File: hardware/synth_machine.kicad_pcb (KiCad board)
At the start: 2 copper layers, 234.9 x 161.9 mm, 90 parts, among them J1 USB-C (MIDI + 5V power), J10 Pot Wave (10k lin, panel moun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, J11 Pot Attack (10k lin, panel mo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, J12 Pot Decay (10k lin, panel mou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, J13 Pot Sustain (10k lin, panel m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, J14 Pot Release (10k lin, panel m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, J3 Panel power switch, J4 From amp screw terminals (L+ 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, J5 Speaker L (JST-PH), J6 Speaker R (JST-PH), J7 Headphones 3.5mm (CUI SJ1-351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, J8 Expansion, J9 Panel LED (anode, cathode), Q1 2N3904, SW1 KEY C4 (direct D10) - 2x Keys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, SW10 D#4 [c4 r1] - 2x Keystone 3534, SW11 F#4 [c3 r1] - 2x Keystone 3534, SW12 G#4 [c2 r1] - 2x Keystone 3534, SW13 A#4 [c1 r1] - 2x Keystone 3534, SW14 BTN1 [c0 r0] - 2x Keystone 35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, SW15 BTN2 [c0 r1] - 2x Keystone 35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, SW16 BTN3 [c1 r0] - 2x Keystone 35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, SW17 BTN4 [c2 r0] - 2x Keystone 35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, SW18 BTN5 [c3 r0] - 2x Keystone 35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, SW19 BTN6 [c4 r0] - 2x Keystone 35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, SW2 D4 [c5 r1] - 2x Keystone 3534, SW3 E4 [c5 r2] - 2x Keystone 3534, SW4 F4 [c4 r2] - 2x Keystone 3534, SW5 G4 [c3 r2] - 2x Keystone 3534, SW6 A4 [c2 r2] - 2x Keystone 3534, SW7 B4 [c1 r2] - 2x Keystone 3534, SW8 C5 [c0 r2] - 2x Keystone 3534, SW9 C#4 [c5 r0] - 2x Keystone 3534, U1 Daisy Seed, U2 TPA6138A2PWR

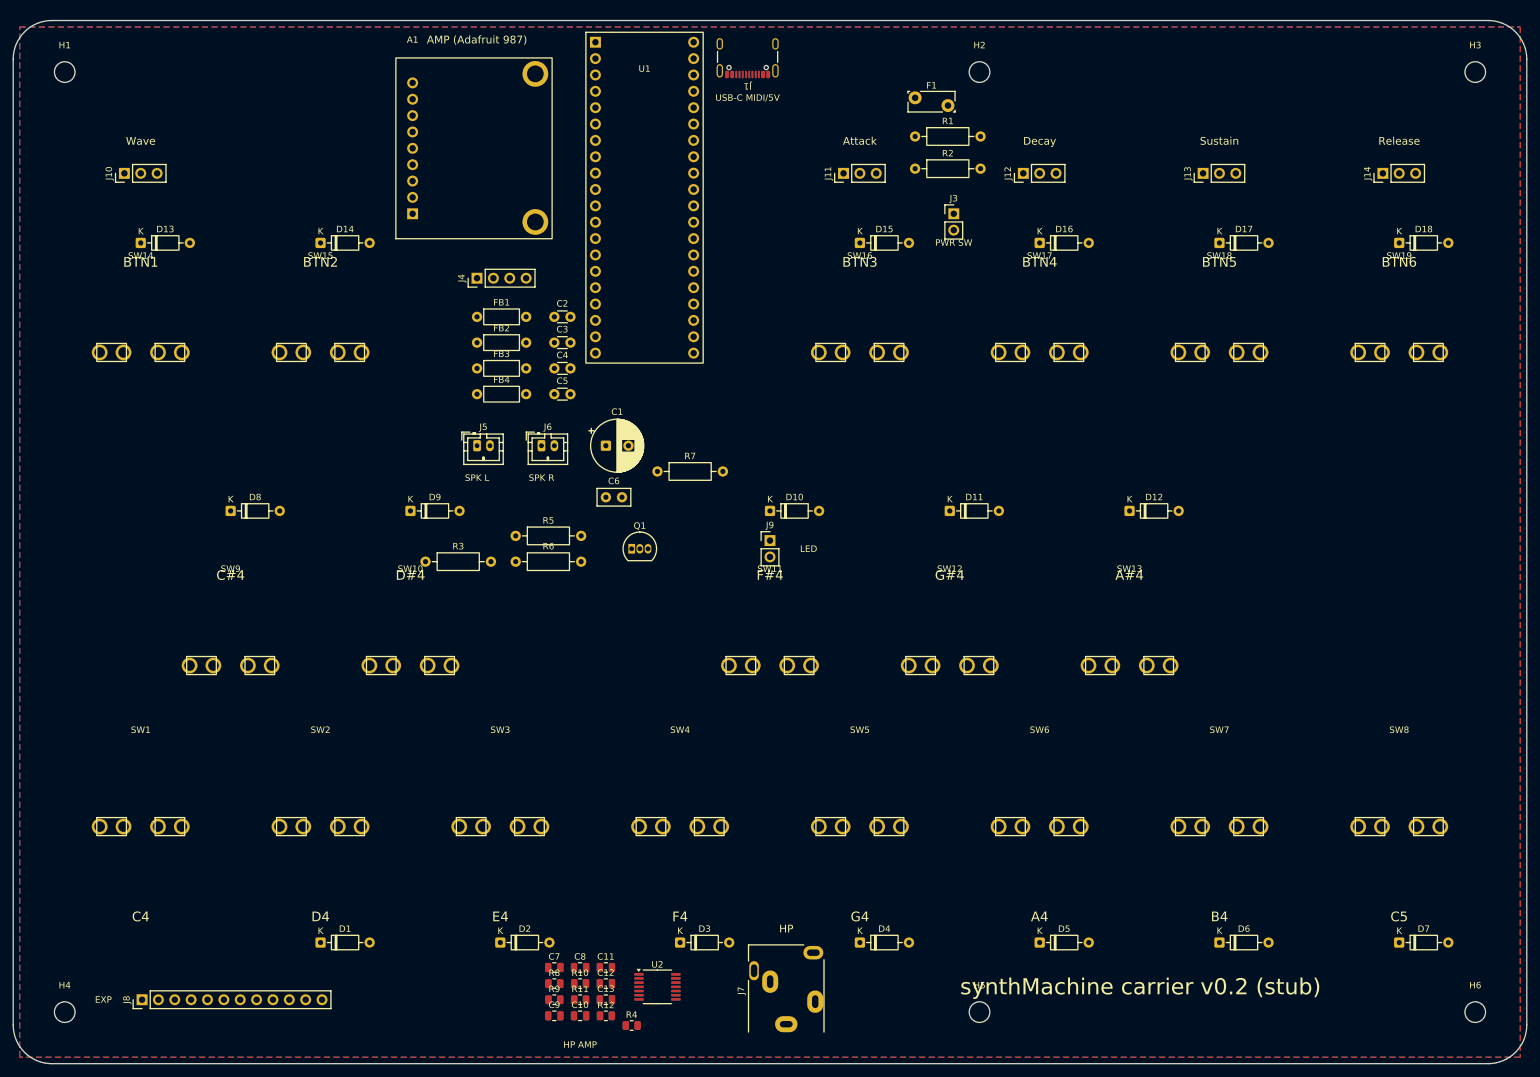
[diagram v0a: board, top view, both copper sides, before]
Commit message: Route the carrier board and fix the button tab pitch
- Button tab pitch measured 9.05 mm outer-to-outer (2.8 mm tabs), so the
  Keystone 3534 receptacle pairs now sit on 6.25 mm centres
- hardware/route.py: Specctra export -> Freerouting (headless, Java 25) ->
  session import -> GND pours on both layers -> fill.  Pours are stripped
  before export so GND is routed with real tracks/vias
- Net classes: 0.25 mm default, 0.6 mm Power (+5V, speaker lines),
  0.4 mm USB_Power for VBUS
- Board is fully routed: 781 segments, 46 vias, 0 unrouted, DRC clean
  apart from USB-C library hole-clearance nits and two thermal-spoke notes

Co-Authored-By: Claude Fable 5.1 <noreply@anthropic.com>
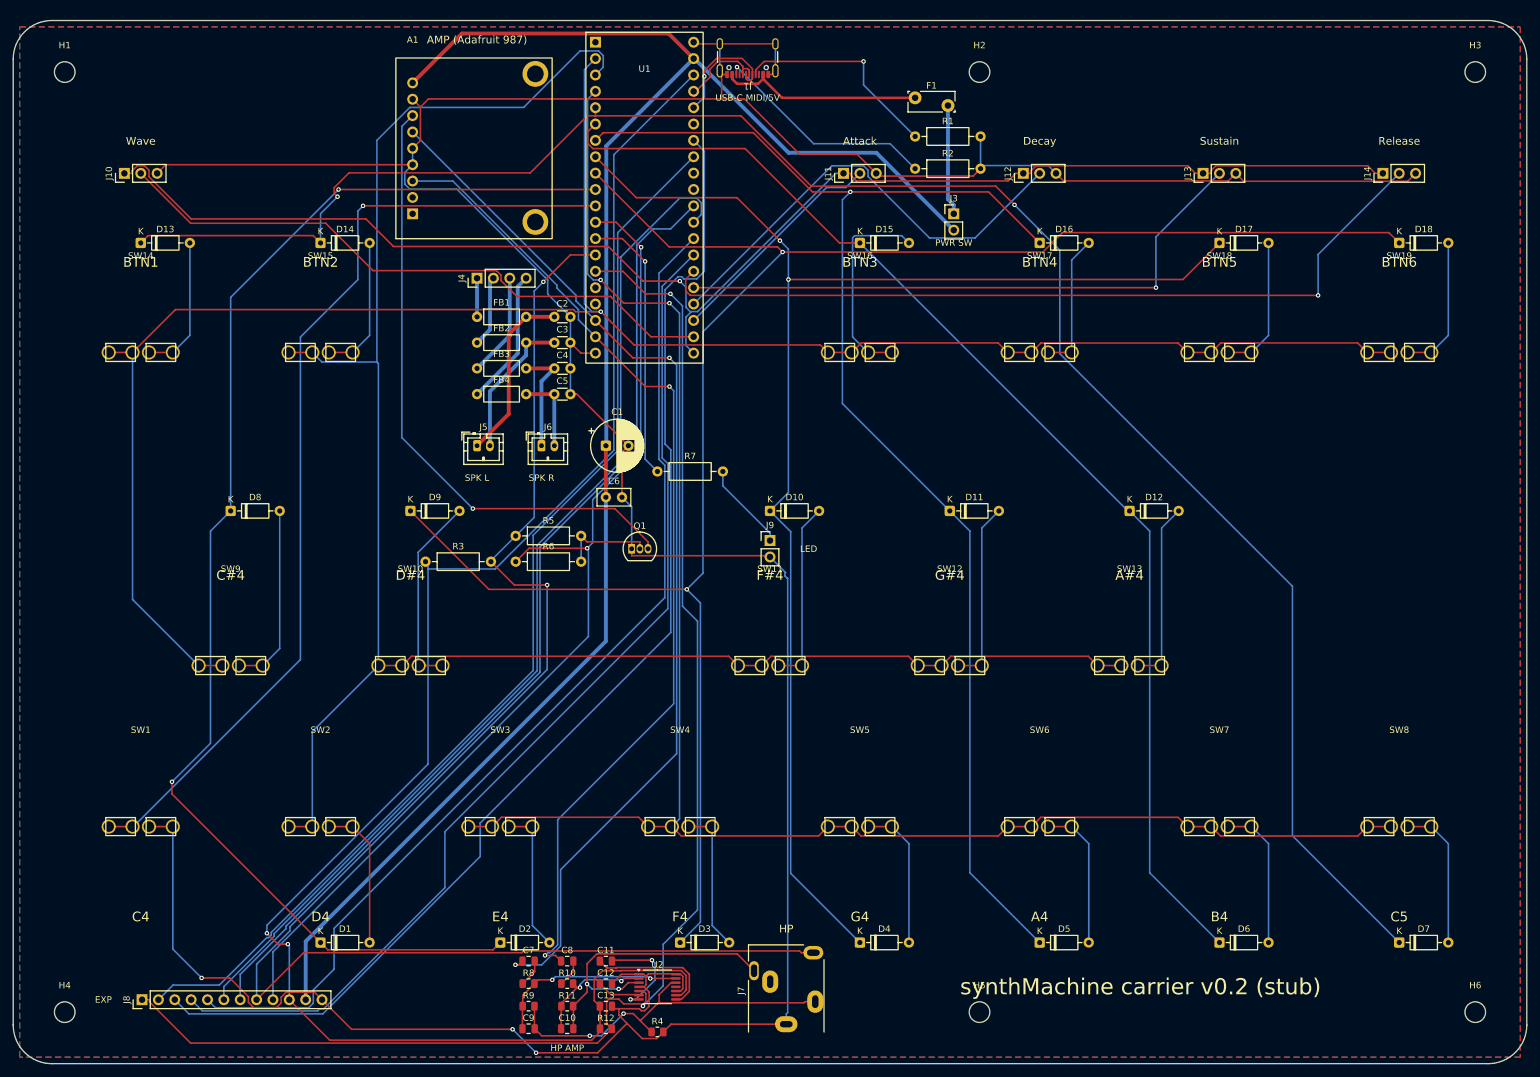
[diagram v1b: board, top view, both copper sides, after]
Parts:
- moved C9 4.47 mm to (80.0, 156.5)
- moved C7 4.12 mm to (80.0, 146.0)
- moved R4 4.12 mm to (100.0, 157.0)
- moved R9 4.12 mm to (80.0, 153.0)
- moved R8 4.00 mm to (80.0, 149.5)
- moved C10 2.83 mm to (86.0, 156.5)
- moved C8 2.24 mm to (86.0, 146.0)
- moved R11 2.24 mm to (86.0, 153.0)
- moved R10 2.00 mm to (86.0, 149.5)
- moved R12 2.00 mm to (92.0, 156.5)
- moved C11 1.00 mm to (92.0, 146.0)
- moved C13 1.00 mm to (92.0, 153.0)
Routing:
- net GND: track 0.00 -> 590.3 mm, vias 0 -> 3
- net ROW0: track 0.00 -> 306.6 mm, vias 0 -> 1
- net COL4: track 0.00 -> 295.2 mm, vias 0 -> 2
- net COL0: track 0.00 -> 295.2 mm, vias 0 -> 2
- net ROW1: track 0.00 -> 292.5 mm
- net ROW2: track 0.00 -> 275.1 mm, vias 0 -> 2
- net +5V: track 0.00 -> 270.9 mm
- net +3V3: track 0.00 -> 260.0 mm, vias 0 -> 2
- net HP_DET: track 0.00 -> 239.6 mm, vias 0 -> 2
- net +3.3VA: track 0.00 -> 227.5 mm, vias 0 -> 1
- net HP_MUTE: track 0.00 -> 219.8 mm, vias 0 -> 2
- net COL3: track 0.00 -> 219.8 mm, vias 0 -> 2
- net COL2: track 0.00 -> 206.3 mm, vias 0 -> 1
- net COL5: track 0.00 -> 205.9 mm, vias 0 -> 2
- net EXP_D27: track 0.00 -> 187.6 mm
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
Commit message: Seat the USB-C receptacle on the board edge, harden route.py
- J1 moved so the footprint's "PCB Edge" guide line sits on the outline
  (shell overhangs ~1 mm as intended); board re-routed, still 0 unrouted
- route.py runs the pour step in a fresh interpreter (SWIG ownership crash
  when reloading the board in the same process)
- README: connector-edge check added to the pre-order list

Co-Authored-By: Claude Fable 5.1 <noreply@anthropic.com>
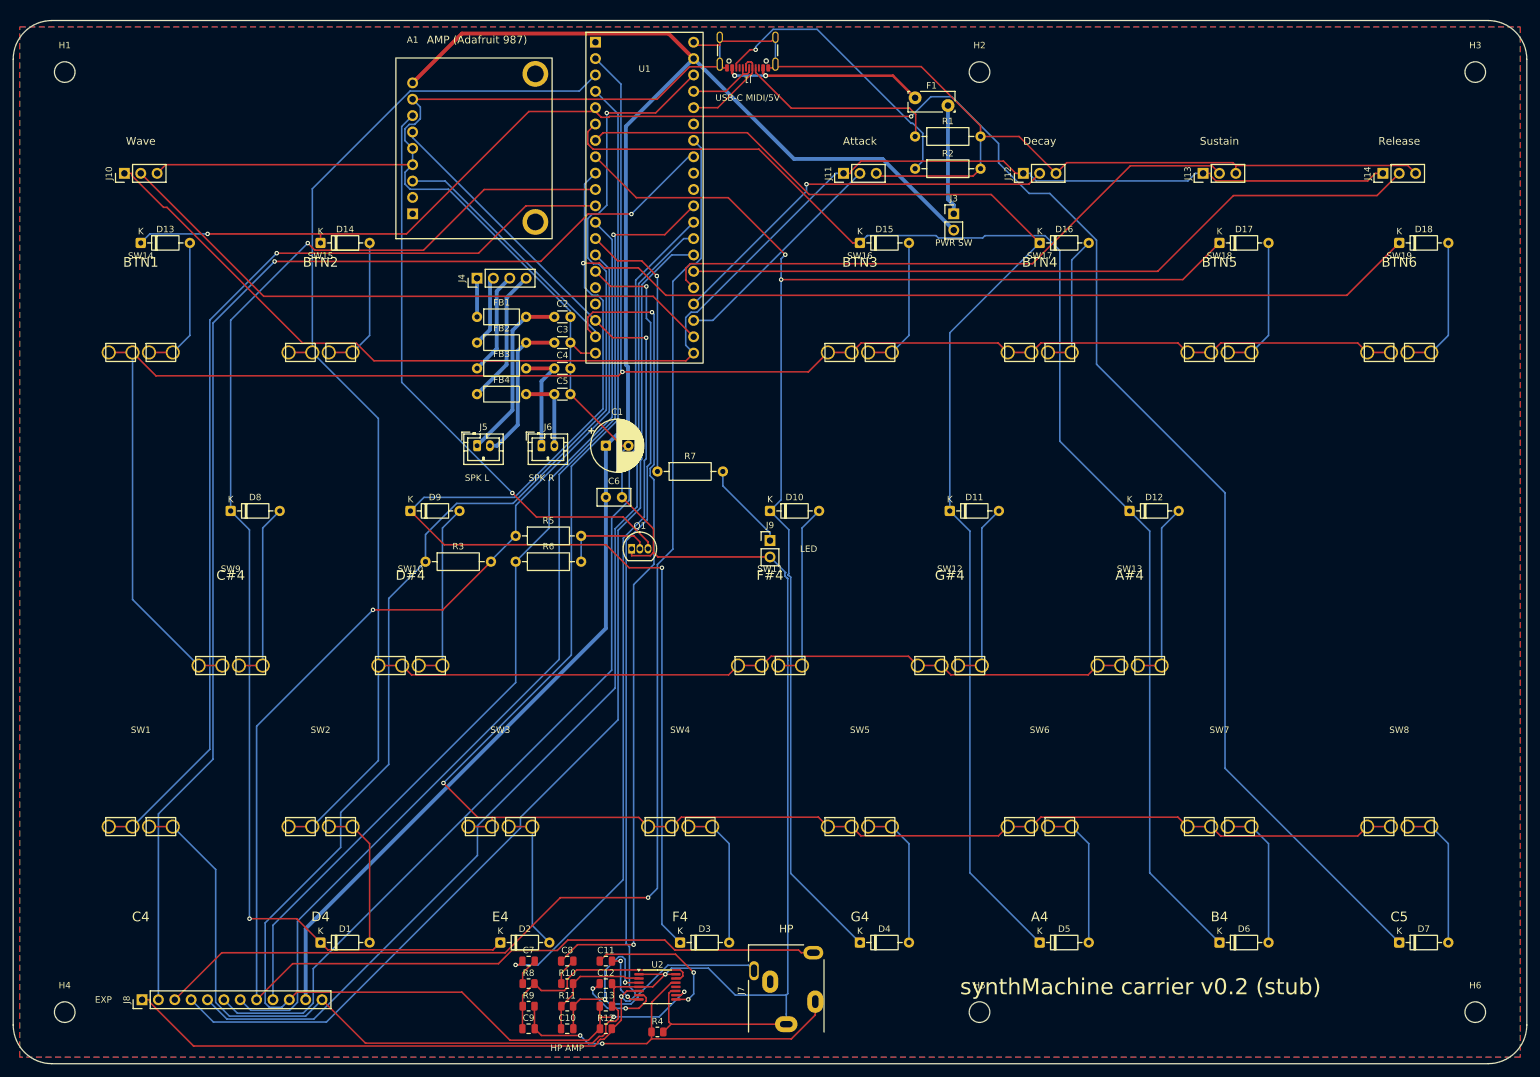
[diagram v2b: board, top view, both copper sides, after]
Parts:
- moved J1 1.03 mm to (114.0, 3.67)
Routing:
- net EXP_D26: track 169.6 -> 193.8 mm, vias 0 -> 2
- net GND: track 590.3 -> 613.7 mm, vias 3 -> 1
- net COL1: track 184.0 -> 202.6 mm
- net MUTE: track 161.3 -> 143.6 mm, vias 2 -> 0
- net COL4: track 295.2 -> 309.8 mm
- net EXP_D27: track 187.6 -> 202.0 mm, vias 0 -> 1
- net AUDIO_R: track 154.2 -> 165.1 mm
- net POT_RELEASE: track 126.2 -> 115.8 mm, vias 1 -> 0
- net EXP_A8: track 154.0 -> 164.1 mm, vias 0 -> 1
- net KBTN3_D: track 31.9 -> 21.8 mm
- net COL2: track 206.3 -> 196.7 mm, vias 1 -> 0
- net CC2: track 35.4 -> 44.8 mm
- net HP_MUTE: track 219.8 -> 210.5 mm
- net POT_DECAY: track 72.0 -> 62.8 mm, vias 0 -> 1
- net ROW1: track 292.5 -> 285.1 mm
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
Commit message: Hand-route the audio nets, move headphone amp and jack to the left edge
- PREROUTES in gen_kicad.py: AUDIO_L/R from the Seed line out to the amp
  header (nested L shapes, F.Cu) and to the headphone amp input caps
  (B.Cu with a via at each cap), 0.3 mm, laid down locked by route.py before
  Freerouting so the autorouter works around them; verified 18/18 kept
- Headphone amp cluster and jack relocated to the left edge between BTN1 and
  C#4, shrinking the audio runs from ~100 mm to ~20 mm
- Speaker EMI caps moved left of the ferrite beads, out of the audio path
- route.py keeps removed tracks/zones referenced (pcbnew crashes otherwise)
- Board: 770 segments, 48 vias, 0 unrouted, DRC clean apart from known nits

Co-Authored-By: Claude Fable 5.1 <noreply@anthropic.com>
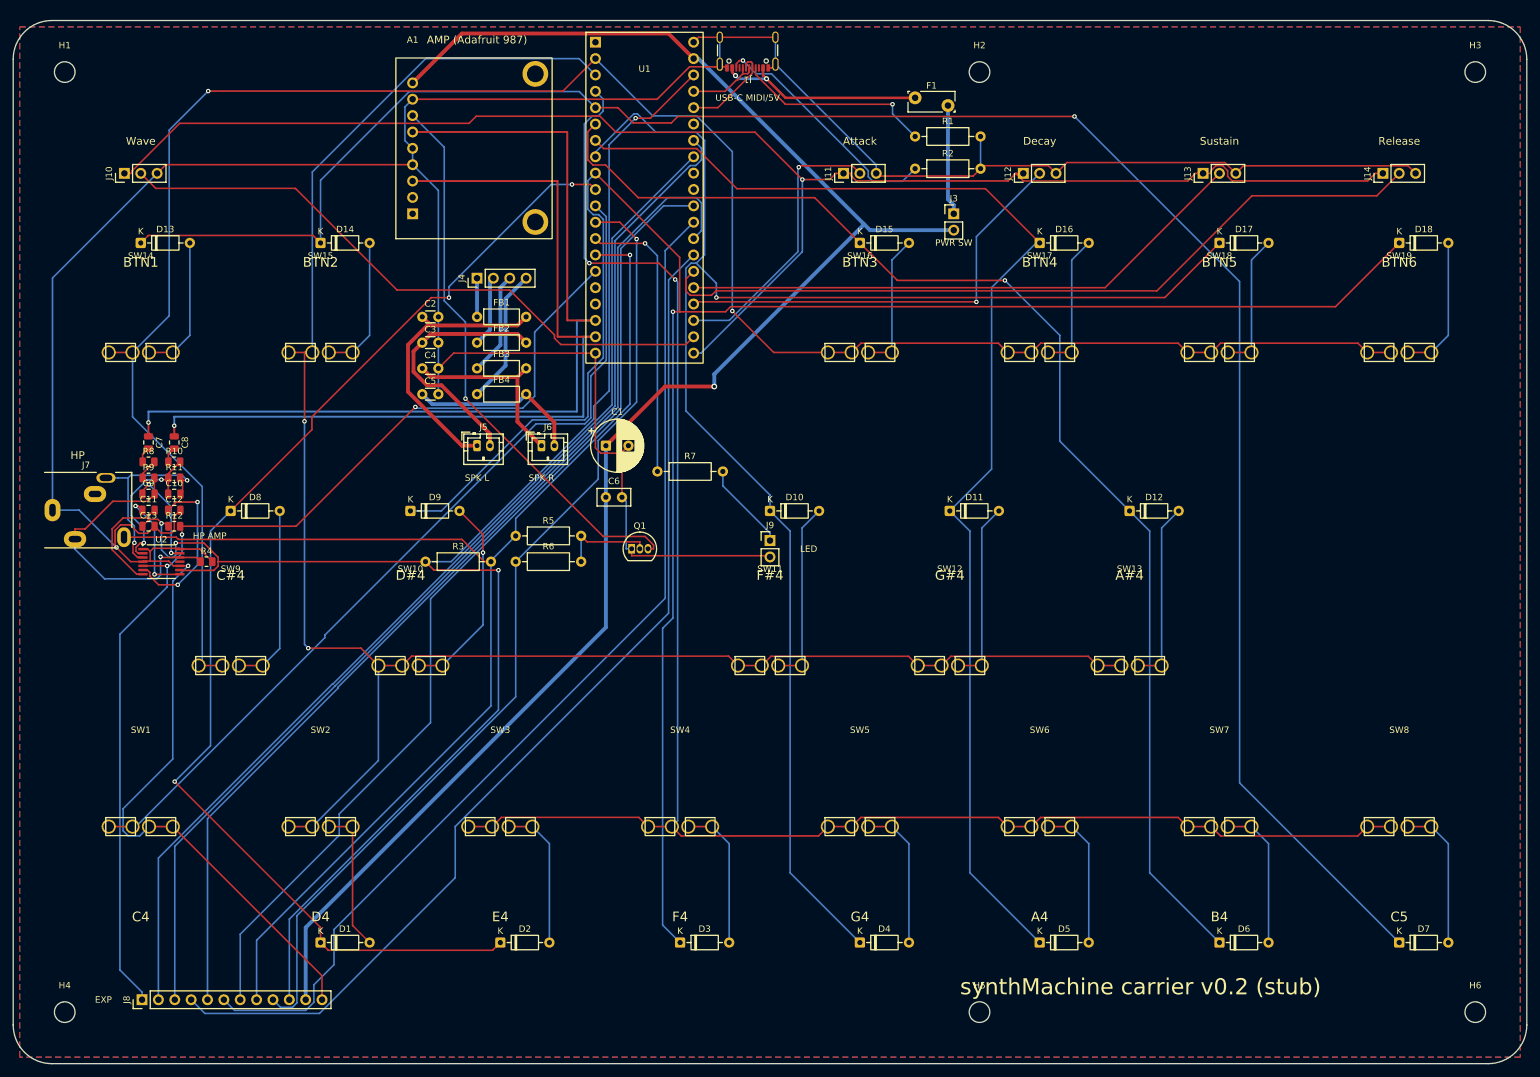
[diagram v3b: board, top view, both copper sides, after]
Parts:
- moved J7 139.1 mm to (6.10, 76.0), turned to 0 degrees
- moved C10 103.0 mm to (25.0, 73.5)
- moved C13 102.9 mm to (21.0, 78.5)
- moved R12 102.8 mm to (25.0, 78.5)
- moved R11 102.2 mm to (25.0, 71.0)
- moved C9 101.8 mm to (21.0, 73.5)
- moved U2 101.4 mm to (23.0, 84.0)
- moved R10 101.4 mm to (25.0, 68.5)
- moved R4 101.1 mm to (30.0, 84.0)
- moved R9 101.0 mm to (21.0, 71.0)
- moved C8 101.0 mm to (25.0, 65.5), turned to -90 degrees
- moved R8 100.2 mm to (21.0, 68.5)
- moved C7 99.8 mm to (21.0, 65.5), turned to -90 degrees
- moved C11 99.7 mm to (21.0, 76.0)
- moved C12 99.5 mm to (25.0, 76.0)
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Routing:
- net GND: track 613.7 -> 568.9 mm, vias 1 -> 2
- net HP_MUTE: track 210.5 -> 169.8 mm, vias 2 -> 3
- net EXP_D27: track 202.0 -> 168.3 mm, vias 1 -> 0
- net HP_DET: track 236.6 -> 203.5 mm
- net AUDIO_R: track 165.1 -> 133.4 mm, vias 2 -> 1
- net EXP_D26: track 193.8 -> 165.3 mm, vias 2 -> 0
- net COL3: track 219.9 -> 247.4 mm, vias 2 -> 1
- net HP_R: track 49.8 -> 30.6 mm
- net KEY_C4: track 154.5 -> 135.9 mm, vias 1 -> 0
- net HP_L: track 62.6 -> 45.0 mm, vias 2 -> 1
- net SPKF_L-: track 23.4 -> 40.0 mm
- net ROW0: track 312.6 -> 328.8 mm, vias 1 -> 2
- net SPKF_L+: track 27.5 -> 43.3 mm
- net +3.3VA: track 228.8 -> 244.4 mm, vias 0 -> 1
- net HP_INL: track 35.3 -> 20.0 mm, vias 0 -> 2
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
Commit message: Drop the panel power switch and LED header; KiCad 10 compatibility
- J3 removed: the polyfuse now feeds +5V directly (unplug USB to power off)
- J9/R7 removed, D12 is free again
- USB-C shield pad is "SH" in the KiCad 10 footprint library (was S1); the
  generator maps both so the shield stays on GND
- re-routed with the locked audio pre-routes: 805 segments, 48 vias, 0 unrouted

Co-Authored-By: Claude Fable 5.1 <noreply@anthropic.com>
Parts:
- removed J3: Panel power switch, PinHeader_1x02_P2.54mm_Vertical
- removed J9: Panel LED (anode, cathode), PinHeader_1x02_P2.54mm_Vertical
- removed R7: 1k, R_Axial_DIN0207_L6.3mm_D2.5mm_P10.16mm_Horizontal
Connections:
- F1 pad 2: +5V_SW -> +5V
- U1 pad 13: LED -> (no net)
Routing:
- net POT_WAVE: track 97.6 -> 167.7 mm
- net EXP_D26: track 165.3 -> 211.2 mm, vias 0 -> 1
- net LED: track 44.2 -> 0.00 mm, vias 1 -> 0
- net COL3: track 247.4 -> 219.8 mm
- net GND: track 568.9 -> 545.3 mm, vias 2 -> 1
- net +5V: track 260.6 -> 281.5 mm
- net COL5: track 189.0 -> 207.0 mm, vias 3 -> 2
- net +5V_SW: track 17.2 -> 0.00 mm
- net POT_DECAY: track 68.1 -> 84.9 mm
- net SPKF_R+: track 29.4 -> 44.7 mm
- net SPKF_R-: track 27.2 -> 41.9 mm
- net COL1: track 195.1 -> 180.9 mm, vias 1 -> 0
- net LED_A: track 13.8 -> 0.00 mm
- net AMP_SD: track 87.4 -> 100.3 mm
- net EXP_A6: track 165.7 -> 178.1 mm
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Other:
- board text removed: "LED"
- board text removed: "PWR SW"
